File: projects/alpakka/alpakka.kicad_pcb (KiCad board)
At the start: 2 copper layers, 130 x 51 mm, 94 parts, among them P1 Debug, P2 Endpoint, P3 Conn_01x02, Q1 Q_PMOS_DGS, U1 Raspberry_Pico, U10 ST_LSM6, U12 ST_LSM6, U2 Alpsalpine_RKJXV, U3 Alpsalpine_EC10E, U4 Alpsalpine_RKJXM, U6 NXP_PCAL6416A, U8 NXP_PCAL6416A

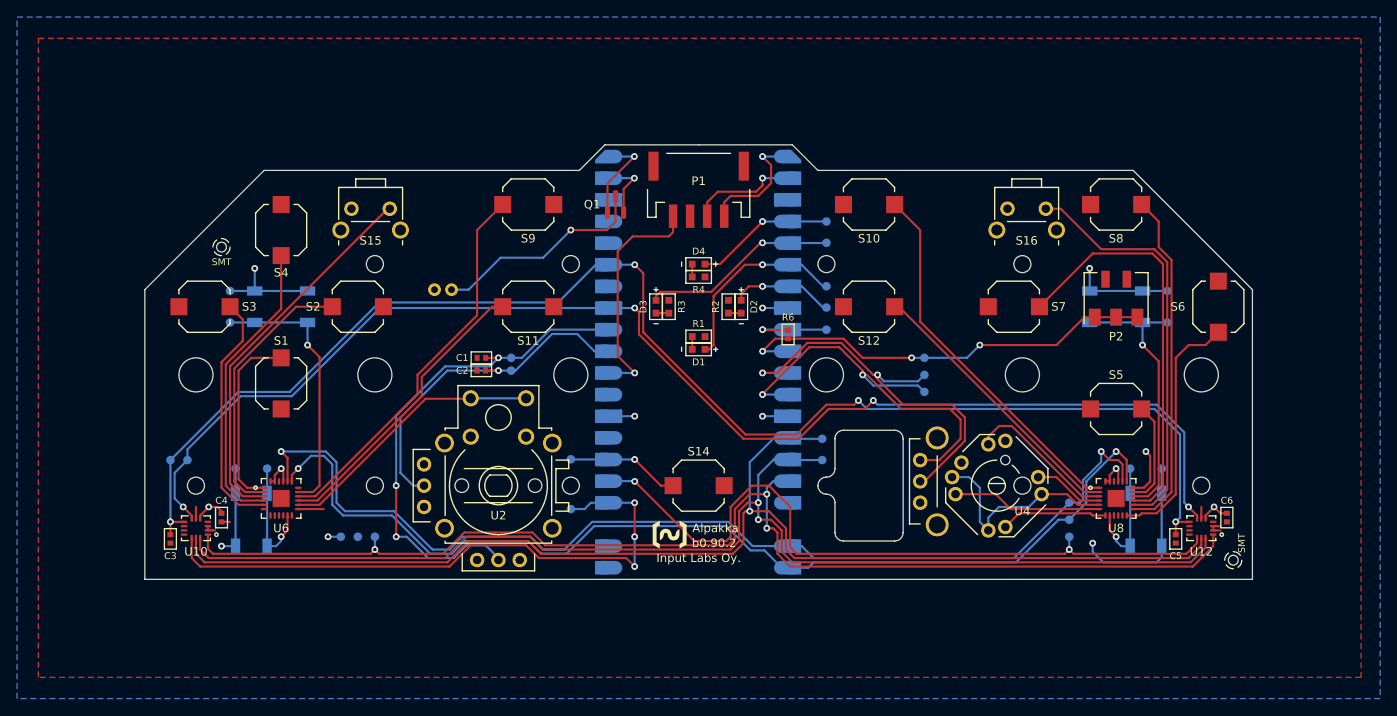
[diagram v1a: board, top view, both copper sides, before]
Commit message: add joystick 3d model and order info
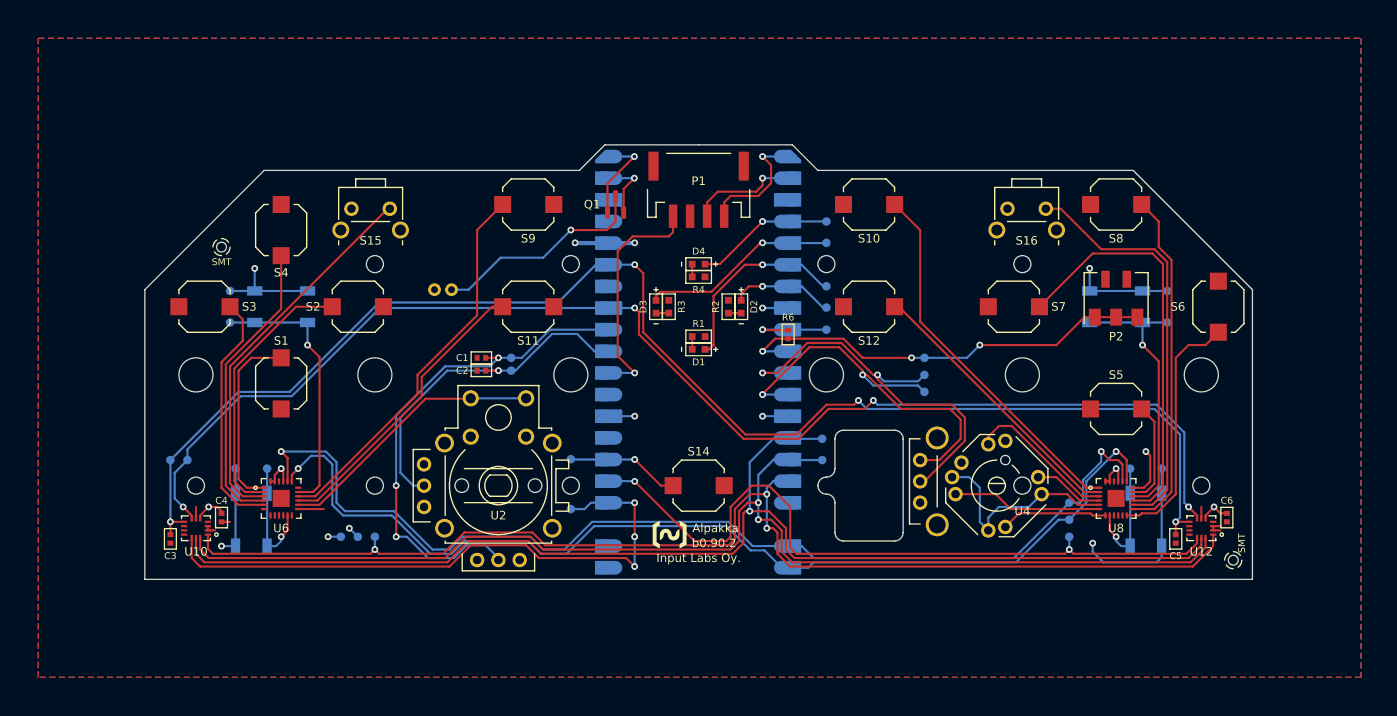
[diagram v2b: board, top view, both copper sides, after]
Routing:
- net VCC: track 22.2 -> 30.7 mm, vias 5 -> 8
- added copper zone on B.Cu, net GND
- added copper zone on In1.Cu, net GND
- added copper zone on In2.Cu, net VCC
- removed copper zone on B.Cu, net VCC
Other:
- copper layers 2 -> 4

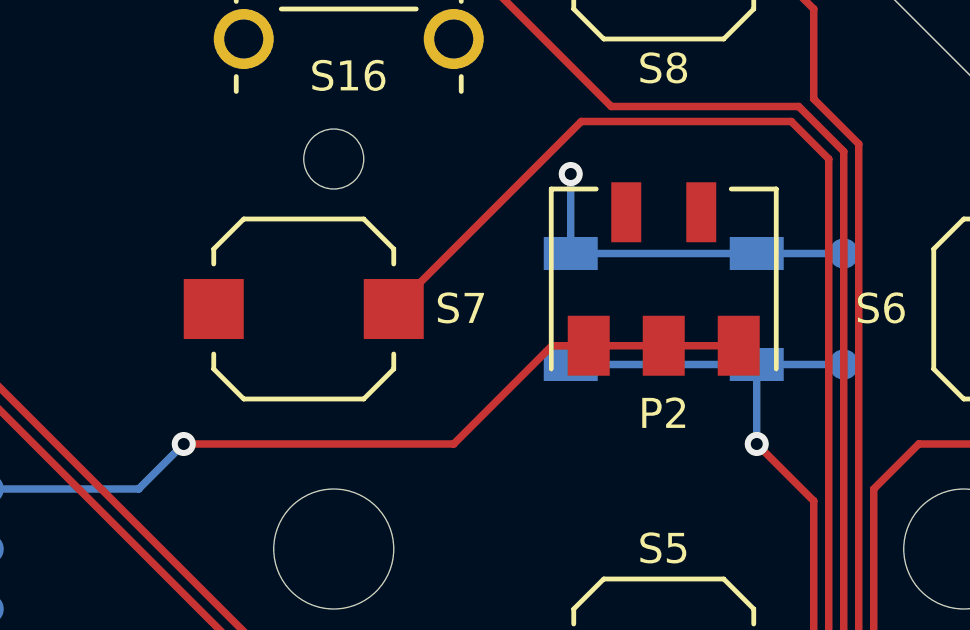
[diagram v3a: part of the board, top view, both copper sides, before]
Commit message: replace capacitive contact part with one with 3d model
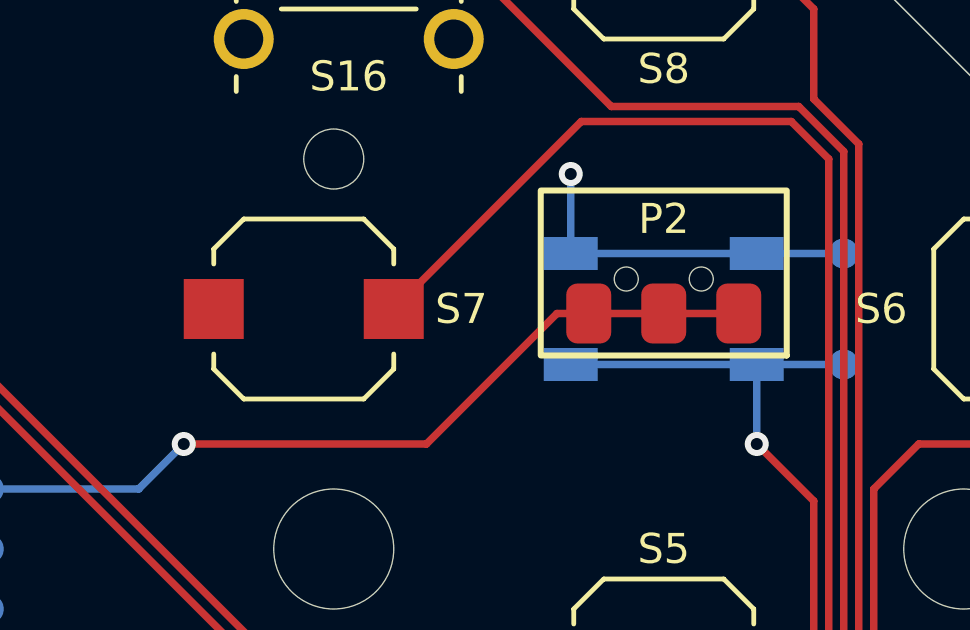
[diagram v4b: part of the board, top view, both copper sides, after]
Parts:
- P2: footprint ILO_fp:HRO_BC-25-3P -> ILO_fp:304D-262503
- U6, U8: value NXP_PCAL6416A -> PCAL6416A
- turned P2 to 180 degrees
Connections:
- net /A10 renamed A10
- U6 pad 13: GND -> A11
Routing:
- net GND: track 77.5 -> 74.5 mm
- net A11: track 0.00 -> 3.00 mm

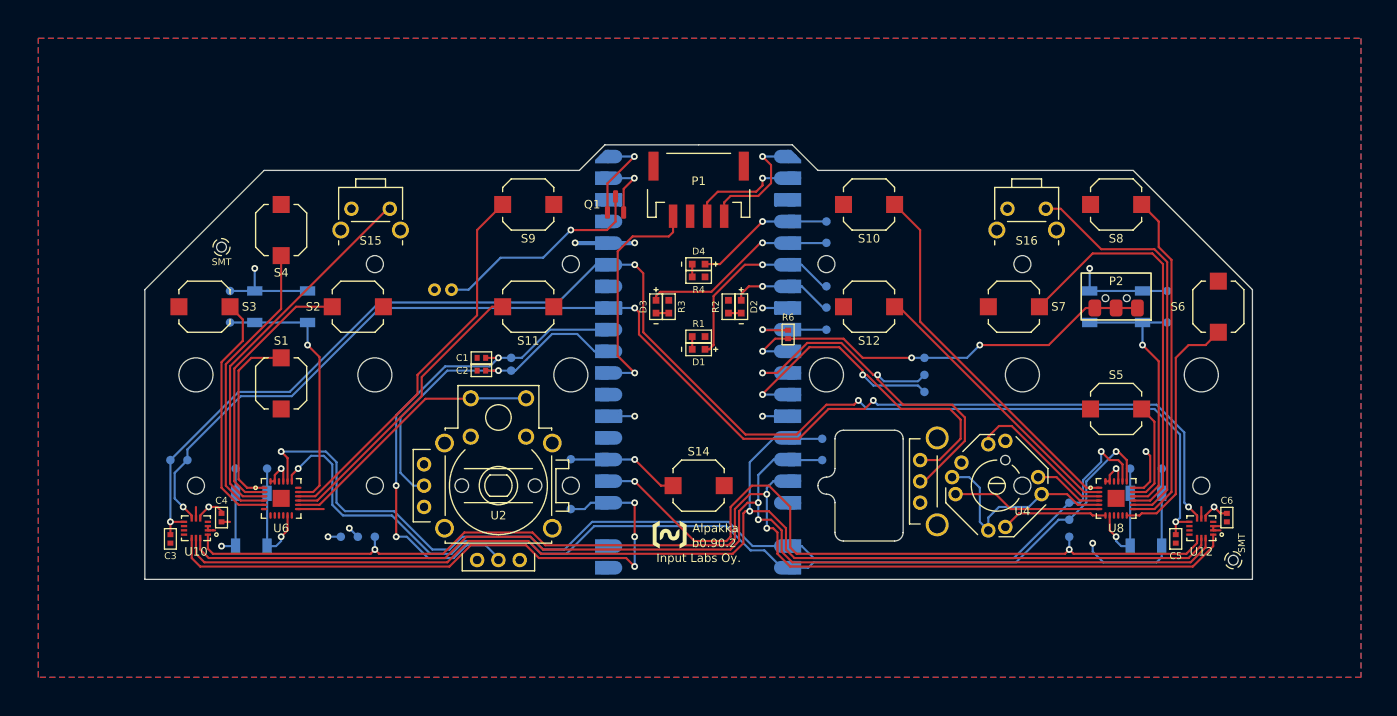
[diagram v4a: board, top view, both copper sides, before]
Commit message: add resistor order info
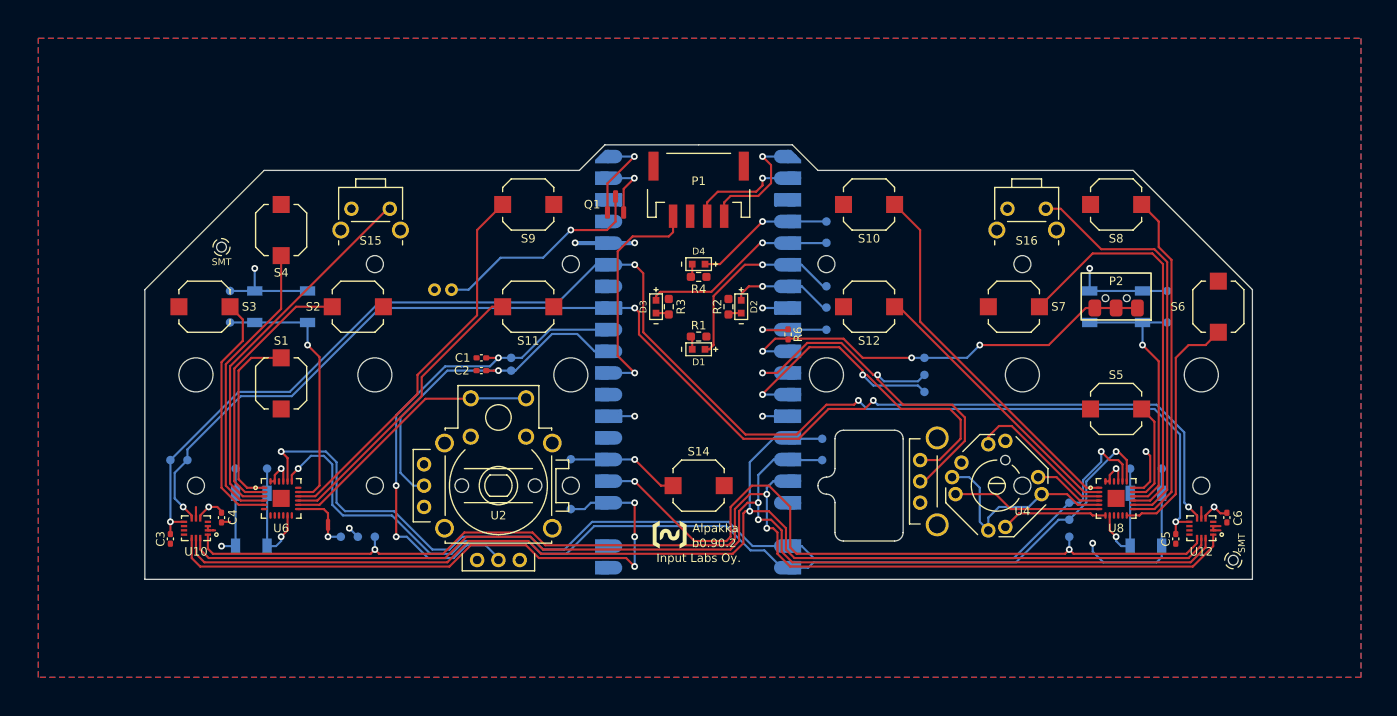
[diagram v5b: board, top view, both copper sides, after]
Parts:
- added NT1: NetTie, NetTie:NetTie-2_SMD_Pad0.5mm, F.Cu at (56.5, 79.6)
- C1, C2, C3, C4, C5, C6: footprint ILO_fp:0402 -> Capacitor_SMD:C_0402_1005Metric_Pad0.74x0.62mm_HandSolder
- R1, R2, R3, R4: footprint ILO_fp:0603 -> Resistor_SMD:R_0603_1608Metric_Pad0.98x0.95mm_HandSolder
- R6: footprint ILO_fp:0402 -> Resistor_SMD:R_0402_1005Metric_Pad0.72x0.64mm_HandSolder
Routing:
- net A11: track 3.00 -> 4.56 mm
- net GND: track 74.5 -> 75.4 mm

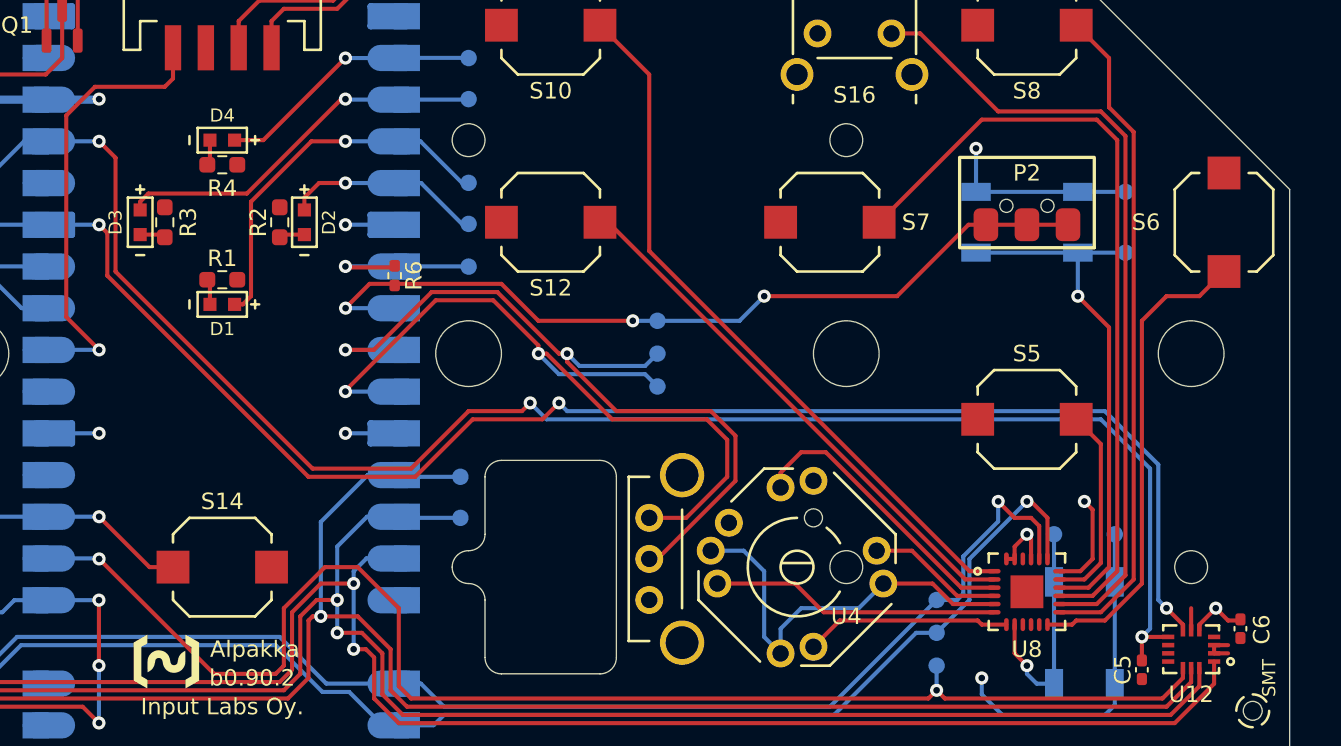
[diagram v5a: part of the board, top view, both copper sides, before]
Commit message: mod button keepout zone
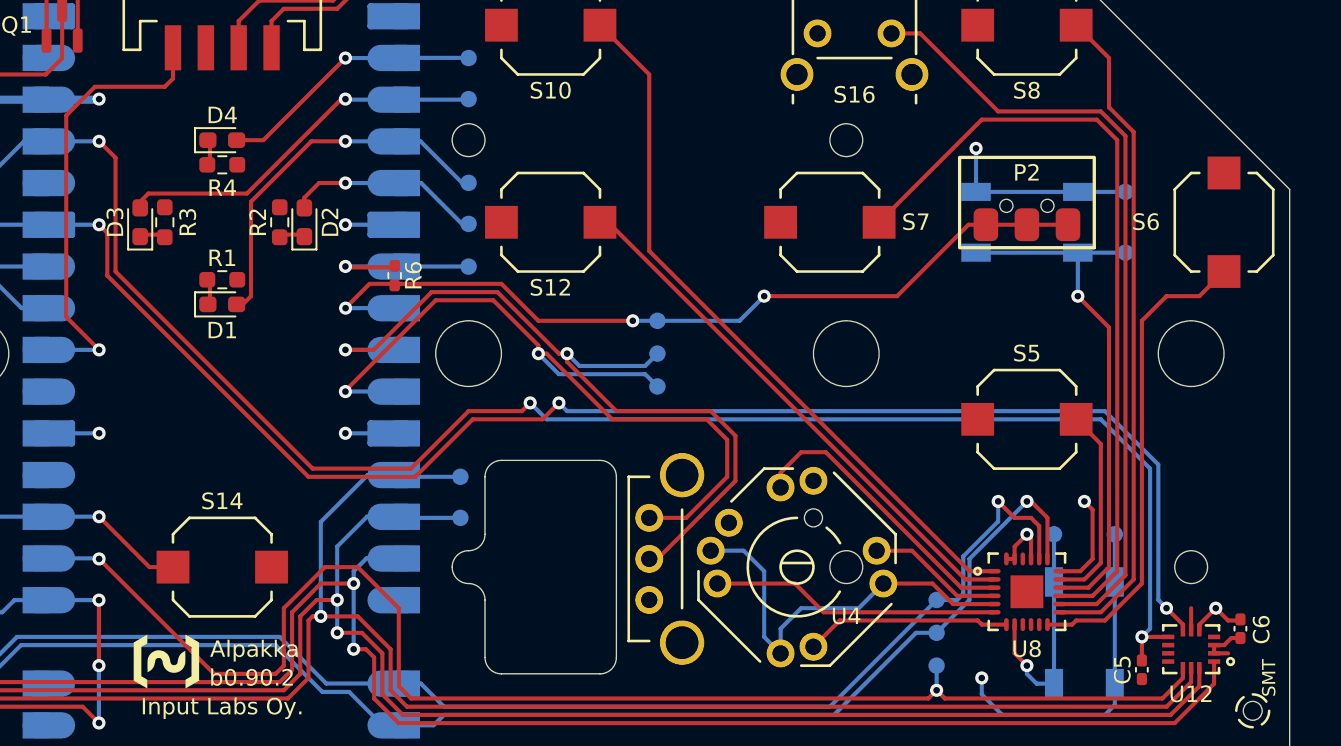
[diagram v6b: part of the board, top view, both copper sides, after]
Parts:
- D1, D2, D3, D4: footprint ILO_fp:0603_d -> Diode_SMD:D_0603_1608Metric_Pad1.05x0.95mm_HandSolder
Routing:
- net GND: track 75.4 -> 76.3 mm

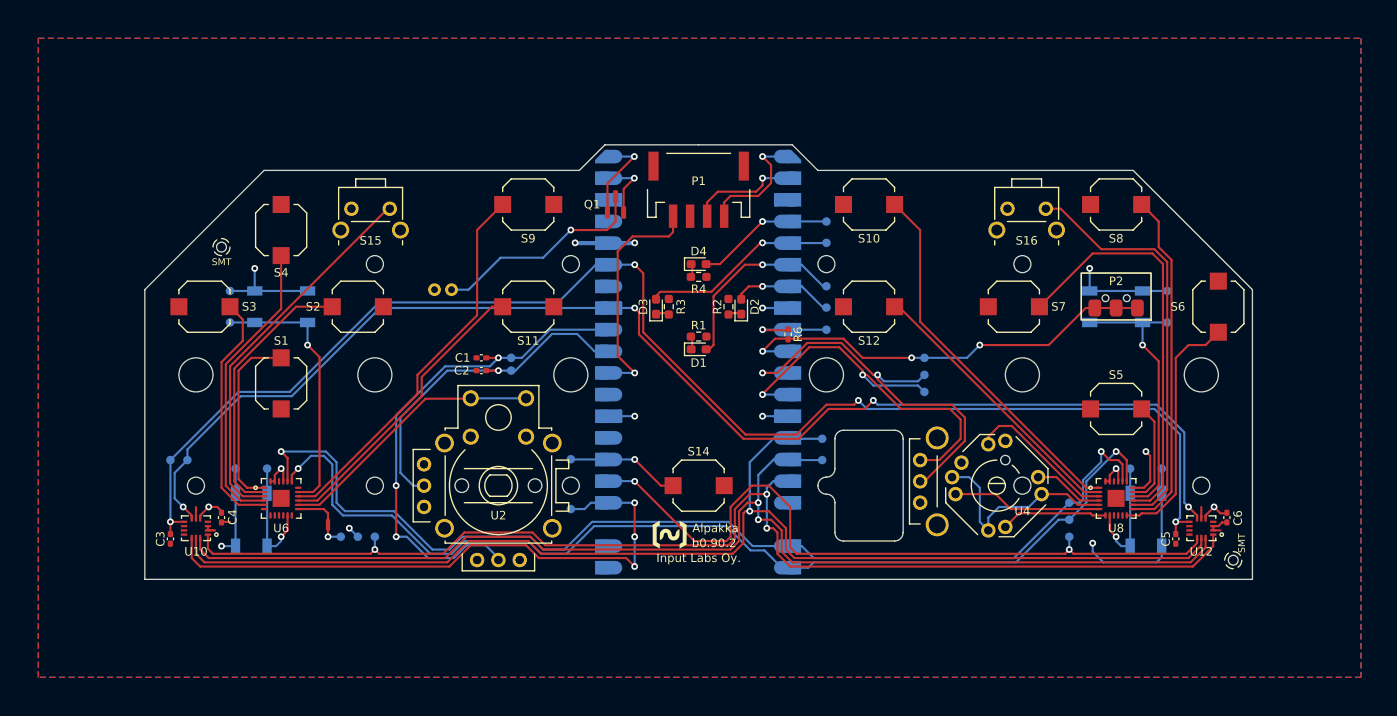
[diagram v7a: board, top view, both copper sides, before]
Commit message: add Rpi Pico 3d model, also other mods
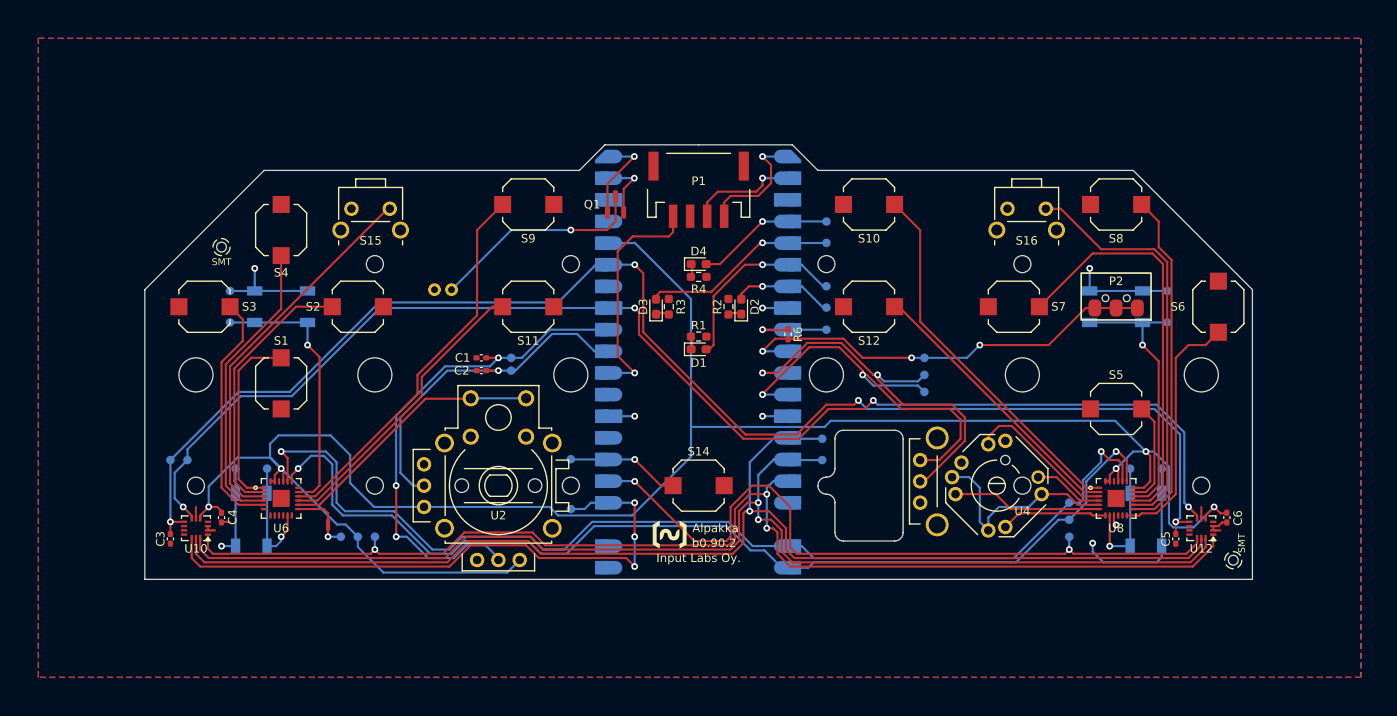
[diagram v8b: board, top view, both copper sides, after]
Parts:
- C1, C2, C3, C4, C5, C6: value C -> 0.1µF
- H1, H2, H3, H4, H5, H6, H7, H8, H9: renamed from REF**; value NPTH_2mm -> MountingHole2mm
- H10, H11, H12, H13, H14, H15: renamed from REF**; value NPTH_4mm -> MountingHole4mm
- R1, R2, R3, R4: value R -> 20Ω
- R6: value R6 -> 510kΩ
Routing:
- net VCC: track 30.7 -> 239.2 mm, vias 8 -> 5
- net GND: track 76.3 -> 77.5 mm, vias 8 -> 9
- net B7: track 14.2 -> 15.0 mm
- removed copper zone on In1.Cu, net GND
- removed copper zone on In2.Cu, net VCC
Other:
- copper layers 4 -> 2
